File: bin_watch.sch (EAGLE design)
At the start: 100 parts, among them IC1 MEGA48/88/168-MU, J1 USB3100-XX-X_REVB, Q1 32.768kHz, T1 2N7002BKV, T2 2N7002BKV, T3 2N7002BKV, T4 2N7002BKV, T5 PMDT670UPE, T6 PMDT670UPE, T7 PMDT670UPE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

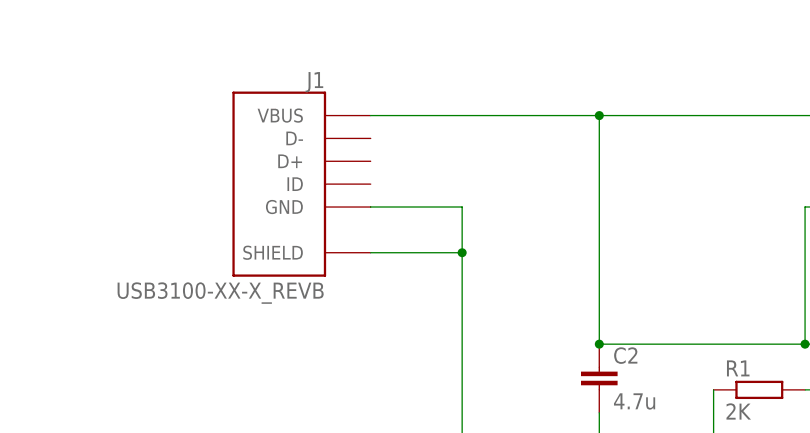
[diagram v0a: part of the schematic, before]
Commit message: Pull resistors for N-channels routed
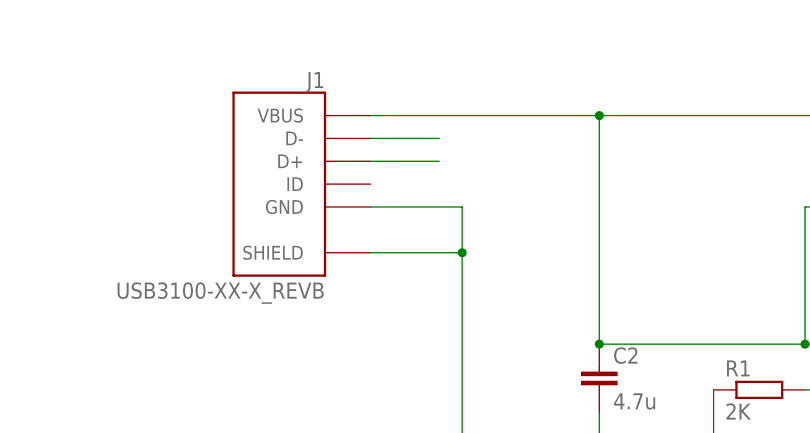
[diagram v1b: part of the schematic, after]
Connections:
- net BLOCK renamed BLOCK5
- net N$1 renamed R_LIGHT5
- net N$2 renamed R_LIGHT6
- net N$4 renamed R_LIGHT7
- net N$5 renamed R_LIGHT4
- net N$6 renamed R_LIGHT0
- net N$7 renamed R_LIGHT1
- net N$8 renamed R_LIGHT2
- net N$9 renamed R_LIGHT3
- net PC0 renamed G_BLOCK0
- net PC1 renamed G_BLOCK1
- net PC2 renamed G_BLOCK2
- net PC3 renamed G_BLOCK3
- net PC4 renamed G_BLOCK4
- net PC5 renamed G_BLOCK5
- net PD0 renamed G_LIGHT0
- net PD1 renamed G_LIGHT1
- net PD2 renamed G_LIGHT2
- net PD3 renamed G_LIGHT3
- net PD4 renamed G_LIGHT4
- net PD5 renamed G_LIGHT5
- net PD6 renamed G_LIGHT6
- net PD7 renamed G_LIGHT7
- new net D_N: J1.D-
- new net D_P: J1.D+
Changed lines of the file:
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@@
 </segment>
 </net>
-<net name="BLOCK" class="3">
+<net name="BLOCK5" class="3">
 <segment>
 <pinref part="D41" gate="G$1" pin="1"/>
@@
 </segment>
 </net>
-<net name="PC0" class="4">
+<net name="G_BLOCK0" class="4">
 <segment>
 <wire x1="139.7" y1="93.98" x2="139.7" y2="106.68" width="0.1524" layer="91"/>
@@
 </segment>
 </net>
-<net name="PC1" class="4">
+<net name="G_BLOCK1" class="4">
 <segment>
 <wire x1="152.4" y1="119.38" x2="152.4" y2="91.44" width="0.1524" layer="91"/>
@@
 </segment>
 </net>
-<net name="PC2" class="4">
+<net name="G_BLOCK2" class="4">
 <segment>
 <wire x1="165.1" y1="106.68" x2="165.1" y2="88.9" width="0.1524" layer="91"/>
@@
 </segment>
 </net>
-<net name="PC3" class="4">
+<net name="G_BLOCK3" class="4">
 <segment>
 <wire x1="177.8" y1="119.38" x2="177.8" y2="86.36" width="0.1524" layer="91"/>
@@
 </segment>
 </net>
-<net name="PC4" class="4">
+<net name="G_BLOCK4" class="4">
 <segment>
 <wire x1="190.5" y1="106.68" x2="190.5" y2="83.82" width="0.1524" layer="91"/>
@@
 </segment>
 </net>
-<net name="PC5" class="4">
+<net name="G_BLOCK5" class="4">
 <segment>
 <wire x1="203.2" y1="119.38" x2="203.2" y2="81.28" width="0.1524" layer="91"/>
@@
 </segment>
 </net>
-<net name="PD0" class="4">
+<net name="G_LIGHT0" class="4">
 <segment>
 <wire x1="177.8" y1="71.12" x2="177.8" y2="43.18" width="0.1524" layer="91"/>
@@
 </segment>
 </net>
-<net name="PD1" class="4">
+<net name="G_LIGHT1" class="4">
 <segment>
 <wire x1="187.96" y1="68.58" x2="187.96" y2="25.4" width="0.1524" layer="91"/>
@@
 </segment>
 </net>
-<net name="PD2" class="4">
+<net name="G_LIGHT2" class="4">
 <segment>
 <wire x1="198.12" y1="66.04" x2="198.12" y2="43.18" width="0.1524" layer="91"/>
@@
 </segment>
 </net>
-<net name="PD3" class="4">
+<net name="G_LIGHT3" class="4">
 <segment>
 <wire x1="208.28" y1="63.5" x2="208.28" y2="25.4" width="0.1524" layer="91"/>
@@
 </segment>
 </net>
-<net name="PD4" class="4">
+<net name="G_LIGHT4" class="4">
 <segment>
 <wire x1="218.44" y1="60.96" x2="218.44" y2="43.18" width="0.1524" layer="91"/>
@@
 </segment>
 </net>
-<net name="PD5" class="4">
+<net name="G_LIGHT5" class="4">
 <segment>
 <wire x1="228.6" y1="58.42" x2="228.6" y2="25.4" width="0.1524" layer="91"/>
@@
 </segment>
 </net>
-<net name="PD6" class="4">
+<net name="G_LIGHT6" class="4">
 <segment>
 <wire x1="238.76" y1="55.88" x2="238.76" y2="43.18" width="0.1524" layer="91"/>
@@
 </segment>
 </net>
-<net name="PD7" class="4">
+<net name="G_LIGHT7" class="4">
 <segment>
 <wire x1="248.92" y1="53.34" x2="248.92" y2="25.4" width="0.1524" layer="91"/>
@@
 </segment>
 </net>
-<net name="N$1" class="0">
+<net name="R_LIGHT5" class="0">
 <segment>
 <wire x1="276.86" y1="58.42" x2="233.68" y2="58.42" width="0.1524" layer="91"/>
@@
 </segment>
 </net>
-<net name="N$2" class="0">
+<net name="R_LIGHT6" class="0">
 <segment>
 <wire x1="261.62" y1="55.88" x2="243.84" y2="55.88" width="0.1524" layer="91"/>
@@
 </segment>
 </net>
-<net name="N$4" class="0">
+<net name="R_LIGHT7" class="0">
 <segment>
 <wire x1="254" y1="33.02" x2="254" y2="53.34" width="0.1524" layer="91"/>
@@
 </segment>
 </net>
-<net name="N$5" class="0">
+<net name="R_LIGHT4" class="0">
 <segment>
 <wire x1="223.52" y1="60.96" x2="269.24" y2="60.96" width="0.1524" layer="91"/>
@@
 </segment>
 </net>
-<net name="N$6" class="0">
+<net name="R_LIGHT0" class="0">
 <segment>
 <pinref part="T1" gate="-1" pin="D"/>
@@
 </segment>
 </net>
-<net name="N$7" class="0">
+<net name="R_LIGHT1" class="0">
 <segment>
 <pinref part="T1" gate="-2" pin="D"/>
@@
 </segment>
 </net>
-<net name="N$8" class="0">
+<net name="R_LIGHT2" class="0">
 <segment>
 <wire x1="203.2" y1="66.04" x2="276.86" y2="66.04" width="0.1524" layer="91"/>
@@
 </segment>
 </net>
-<net name="N$9" class="0">
+<net name="R_LIGHT3" class="0">
 <segment>
 <pinref part="T2" gate="-2" pin="D"/>
@@
 </segment>
 </net>
+<net name="D_N" class="4">
+<segment>
+<pinref part="J1" gate="G$1" pin="D-"/>
+<wire x1="60.96" y1="274.32" x2="68.58" y2="274.32" width="0.1524" layer="91"/>
+</segment>
+</net>
+<net name="D_P" class="4">
+<segment>
+<pinref part="J1" gate="G$1" pin="D+"/>
+<wire x1="60.96" y1="271.78" x2="68.58" y2="271.78" width="0.1524" layer="91"/>
+</segment>
+</net>

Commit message: Pull resistors for N-channels routed
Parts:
- added R19, R20, R21, R22, R23, R24: 1M, rcl:R-EU_R0603
- R13, R14, R15, R16, R17, R18, R2, R3: value 68 -> 1M
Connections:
- net G_BLOCK0: now also R19.1
- net G_BLOCK1: now also R20.1
- net G_BLOCK2: now also R21.1
- net G_BLOCK3: now also R22.1
- net G_BLOCK4: now also R23.1
- net G_BLOCK5: now also R24.1
- net VCC: now also R19.2, R20.2, R21.2, R22.2, R23.2, R24.2
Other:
- moved on the sheet: T5-1, T5-2, T6-1, T6-2, T7-1, T7-2

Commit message: Added solder pads for blocks
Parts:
- removed TP1, TP2, TP3, TP4, TP5, TP6: TPTP07SQ, testpad:TPTP07SQ
- added PAD1, PAD10, PAD11, PAD12, PAD13, PAD14, PAD2, PAD3, PAD4, PAD5, PAD6, PAD7, PAD8, PAD9: (no value), wirepad:SMD2
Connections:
- net BLOCK0: now also PAD9.P
- net BLOCK1: now also PAD10.P
- net BLOCK2: now also PAD11.P
- net BLOCK3: now also PAD12.P
- net BLOCK4: now also PAD13.P
- net BLOCK5: now also PAD14.P
- net GND: no longer TP3.TP
- net LIGHT0: now also PAD1.P
- net LIGHT1: now also PAD2.P
- net LIGHT2: now also PAD3.P
- net LIGHT3: now also PAD4.P
- net LIGHT4: now also PAD5.P
- net LIGHT5: now also PAD6.P
- net LIGHT6: now also PAD7.P
- net LIGHT7: now also PAD8.P
- net MISO: no longer TP6.TP
- net MOSI: no longer TP5.TP
- net RST: no longer TP2.TP
- net SCK: no longer TP4.TP
- net VCC: no longer TP1.TP

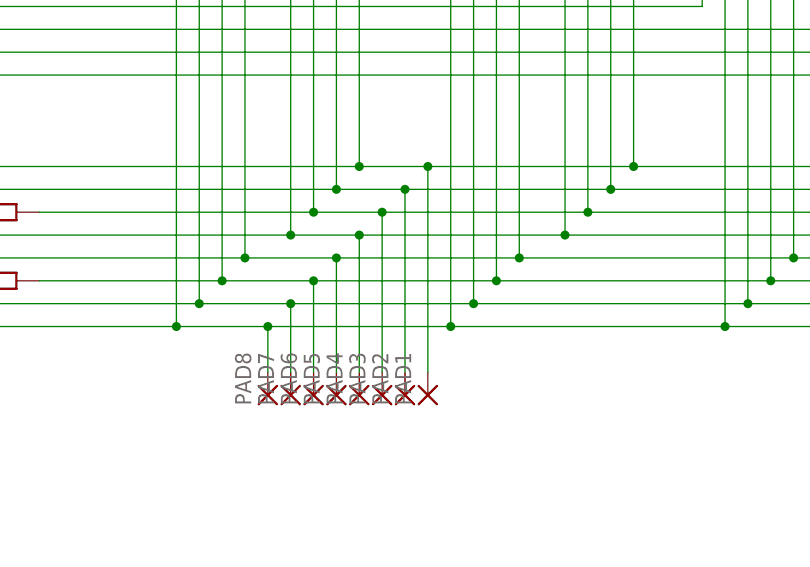
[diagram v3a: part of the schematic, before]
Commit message: Started routing wirepads to drivers
So that the board can be used as a driver for external loads
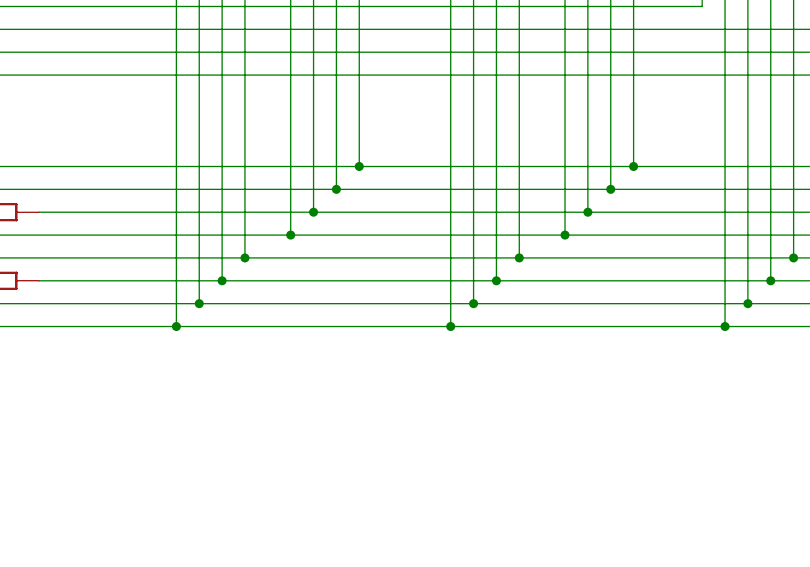
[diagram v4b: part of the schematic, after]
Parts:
- removed PAD1, PAD2, PAD3, PAD4, PAD5, PAD6, PAD7, PAD8: (no value), wirepad:SMD2
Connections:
- net PB0 renamed BTN1
- net PB1 renamed BTN2
- net PB2 renamed BTN3
- net LIGHT0: no longer PAD1.P
- net LIGHT1: no longer PAD2.P
- net LIGHT2: no longer PAD3.P
- net LIGHT3: no longer PAD4.P
- net LIGHT4: no longer PAD5.P
- net LIGHT5: no longer PAD6.P
- net LIGHT6: no longer PAD7.P
- net LIGHT7: no longer PAD8.P
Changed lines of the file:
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@@
 <part name="R24" library="rcl" library_urn="urn:adsk.eagle:library:334" deviceset="R-EU_" device="R0603" package3d_urn="urn:adsk.eagle:package:23555/1" value="1M"/>
 <part name="P+2" library="supply1" library_urn="urn:adsk.eagle:library:371" deviceset="VCC" device=""/>
-<part name="PAD1" library="wirepad" library_urn="urn:adsk.eagle:library:412" deviceset="SMD2" device="" package3d_urn="urn:adsk.eagle:package:30839/1"/>
-<part name="PAD2" library="wirepad" library_urn="urn:adsk.eagle:library:412" deviceset="SMD2" device="" package3d_urn="urn:adsk.eagle:package:30839/1"/>
-<part name="PAD3" library="wirepad" library_urn="urn:adsk.eagle:library:412" deviceset="SMD2" device="" package3d_urn="urn:adsk.eagle:package:30839/1"/>
-<part name="PAD4" library="wirepad" library_urn="urn:adsk.eagle:library:412" deviceset="SMD2" device="" package3d_urn="urn:adsk.eagle:package:30839/1"/>
-<part name="PAD5" library="wirepad" library_urn="urn:adsk.eagle:library:412" deviceset="SMD2" device="" package3d_urn="urn:adsk.eagle:package:30839/1"/>
-<part name="PAD6" library="wirepad" library_urn="urn:adsk.eagle:library:412" deviceset="SMD2" device="" package3d_urn="urn:adsk.eagle:package:30839/1"/>
-<part name="PAD7" library="wirepad" library_urn="urn:adsk.eagle:library:412" deviceset="SMD2" device="" package3d_urn="urn:adsk.eagle:package:30839/1"/>
-<part name="PAD8" library="wirepad" library_urn="urn:adsk.eagle:library:412" deviceset="SMD2" device="" package3d_urn="urn:adsk.eagle:package:30839/1"/>
 <part name="PAD9" library="wirepad" library_urn="urn:adsk.eagle:library:412" deviceset="SMD2" device="" package3d_urn="urn:adsk.eagle:package:30839/1"/>
 <part name="PAD10" library="wirepad" library_urn="urn:adsk.eagle:library:412" deviceset="SMD2" device="" package3d_urn="urn:adsk.eagle:package:30839/1"/>
@@
 <instance part="R24" gate="G$1" x="162.56" y="111.76" rot="R90"/>
 <instance part="P+2" gate="VCC" x="177.8" y="132.08"/>
-<instance part="PAD1" gate="1" x="330.2" y="45.72" rot="R90"/>
-<instance part="PAD2" gate="1" x="327.66" y="45.72" rot="R90"/>
-<instance part="PAD3" gate="1" x="325.12" y="45.72" rot="R90"/>
-<instance part="PAD4" gate="1" x="322.58" y="45.72" rot="R90"/>
-<instance part="PAD5" gate="1" x="320.04" y="45.72" rot="R90"/>
-<instance part="PAD6" gate="1" x="317.5" y="45.72" rot="R90"/>
-<instance part="PAD7" gate="1" x="314.96" y="45.72" rot="R90"/>
-<instance part="PAD8" gate="1" x="312.42" y="45.72" rot="R90"/>
 <instance part="PAD9" gate="1" x="266.7" y="99.06" rot="R270"/>
 <instance part="PAD10" gate="1" x="269.24" y="99.06" rot="R270"/>
@@
 <wire x1="398.78" y1="58.42" x2="368.3" y2="58.42" width="0.1524" layer="91"/>
 <wire x1="368.3" y1="58.42" x2="337.82" y2="58.42" width="0.1524" layer="91"/>
-<wire x1="337.82" y1="58.42" x2="317.5" y2="58.42" width="0.1524" layer="91"/>
-<wire x1="317.5" y1="58.42" x2="307.34" y2="58.42" width="0.1524" layer="91"/>
+<wire x1="337.82" y1="58.42" x2="307.34" y2="58.42" width="0.1524" layer="91"/>
 <wire x1="459.74" y1="111.76" x2="459.74" y2="58.42" width="0.1524" layer="91"/>
 <wire x1="429.26" y1="111.76" x2="429.26" y2="58.42" width="0.1524" layer="91"/>
@@
 <wire x1="307.34" y1="58.42" x2="287.02" y2="58.42" width="0.1524" layer="91"/>
 <pinref part="R10" gate="G$1" pin="2"/>
-<wire x1="317.5" y1="58.42" x2="317.5" y2="48.26" width="0.1524" layer="91"/>
-<junction x="317.5" y="58.42"/>
-<pinref part="PAD6" gate="1" pin="P"/>
 </segment>
 </net>
@@
 <wire x1="396.24" y1="55.88" x2="365.76" y2="55.88" width="0.1524" layer="91"/>
 <wire x1="365.76" y1="55.88" x2="335.28" y2="55.88" width="0.1524" layer="91"/>
-<wire x1="335.28" y1="55.88" x2="314.96" y2="55.88" width="0.1524" layer="91"/>
-<wire x1="314.96" y1="55.88" x2="304.8" y2="55.88" width="0.1524" layer="91"/>
+<wire x1="335.28" y1="55.88" x2="304.8" y2="55.88" width="0.1524" layer="91"/>
 <wire x1="457.2" y1="119.38" x2="457.2" y2="55.88" width="0.1524" layer="91"/>
 <pinref part="D35" gate="G$1" pin="2"/>
@@
 <wire x1="304.8" y1="55.88" x2="271.78" y2="55.88" width="0.1524" layer="91"/>
 <pinref part="R11" gate="G$1" pin="2"/>
-<wire x1="314.96" y1="55.88" x2="314.96" y2="48.26" width="0.1524" layer="91"/>
-<junction x="314.96" y="55.88"/>
-<pinref part="PAD7" gate="1" pin="P"/>
 </segment>
 </net>
@@
 <wire x1="393.7" y1="53.34" x2="363.22" y2="53.34" width="0.1524" layer="91"/>
 <wire x1="363.22" y1="53.34" x2="332.74" y2="53.34" width="0.1524" layer="91"/>
-<wire x1="332.74" y1="53.34" x2="312.42" y2="53.34" width="0.1524" layer="91"/>
-<wire x1="312.42" y1="53.34" x2="302.26" y2="53.34" width="0.1524" layer="91"/>
+<wire x1="332.74" y1="53.34" x2="302.26" y2="53.34" width="0.1524" layer="91"/>
 <wire x1="454.66" y1="127" x2="454.66" y2="53.34" width="0.1524" layer="91"/>
 <wire x1="424.18" y1="127" x2="424.18" y2="53.34" width="0.1524" layer="91"/>
@@
 <wire x1="302.26" y1="53.34" x2="279.4" y2="53.34" width="0.1524" layer="91"/>
 <pinref part="R12" gate="G$1" pin="2"/>
-<wire x1="312.42" y1="53.34" x2="312.42" y2="48.26" width="0.1524" layer="91"/>
-<junction x="312.42" y="53.34"/>
-<pinref part="PAD8" gate="1" pin="P"/>
 </segment>
 </net>
@@
 <wire x1="401.32" y1="60.96" x2="370.84" y2="60.96" width="0.1524" layer="91"/>
 <wire x1="370.84" y1="60.96" x2="340.36" y2="60.96" width="0.1524" layer="91"/>
-<wire x1="340.36" y1="60.96" x2="320.04" y2="60.96" width="0.1524" layer="91"/>
-<wire x1="320.04" y1="60.96" x2="309.88" y2="60.96" width="0.1524" layer="91"/>
+<wire x1="340.36" y1="60.96" x2="309.88" y2="60.96" width="0.1524" layer="91"/>
 <wire x1="462.28" y1="104.14" x2="462.28" y2="60.96" width="0.1524" layer="91"/>
 <pinref part="D33" gate="G$1" pin="2"/>
@@
 <pinref part="R9" gate="G$1" pin="2"/>
 <wire x1="279.4" y1="60.96" x2="309.88" y2="60.96" width="0.1524" layer="91"/>
-<wire x1="320.04" y1="60.96" x2="320.04" y2="48.26" width="0.1524" layer="91"/>
-<junction x="320.04" y="60.96"/>
-<pinref part="PAD5" gate="1" pin="P"/>
 </segment>
 </net>
@@
 <wire x1="414.02" y1="71.12" x2="383.54" y2="71.12" width="0.1524" layer="91"/>
 <wire x1="383.54" y1="71.12" x2="353.06" y2="71.12" width="0.1524" layer="91"/>
-<wire x1="353.06" y1="71.12" x2="330.2" y2="71.12" width="0.1524" layer="91"/>
-<wire x1="330.2" y1="71.12" x2="322.58" y2="71.12" width="0.1524" layer="91"/>
+<wire x1="353.06" y1="71.12" x2="322.58" y2="71.12" width="0.1524" layer="91"/>
 <wire x1="444.5" y1="104.14" x2="444.5" y2="71.12" width="0.1524" layer="91"/>
 <junction x="444.5" y="71.12"/>
@@
 <pinref part="R5" gate="G$1" pin="2"/>
 <wire x1="271.78" y1="71.12" x2="322.58" y2="71.12" width="0.1524" layer="91"/>
-<wire x1="330.2" y1="71.12" x2="330.2" y2="48.26" width="0.1524" layer="91"/>
-<junction x="330.2" y="71.12"/>
-<pinref part="PAD1" gate="1" pin="P"/>
 </segment>
 </net>
@@
 <wire x1="411.48" y1="68.58" x2="381" y2="68.58" width="0.1524" layer="91"/>
 <wire x1="381" y1="68.58" x2="350.52" y2="68.58" width="0.1524" layer="91"/>
-<wire x1="350.52" y1="68.58" x2="327.66" y2="68.58" width="0.1524" layer="91"/>
-<wire x1="327.66" y1="68.58" x2="320.04" y2="68.58" width="0.1524" layer="91"/>
+<wire x1="350.52" y1="68.58" x2="320.04" y2="68.58" width="0.1524" layer="91"/>
 <wire x1="441.96" y1="111.76" x2="441.96" y2="68.58" width="0.1524" layer="91"/>
 <junction x="441.96" y="68.58"/>
@@
 <wire x1="320.04" y1="68.58" x2="279.4" y2="68.58" width="0.1524" layer="91"/>
 <pinref part="R6" gate="G$1" pin="2"/>
-<wire x1="327.66" y1="48.26" x2="327.66" y2="68.58" width="0.1524" layer="91"/>
-<junction x="327.66" y="68.58"/>
-<pinref part="PAD2" gate="1" pin="P"/>
 </segment>
 </net>
@@
 <wire x1="408.94" y1="66.04" x2="378.46" y2="66.04" width="0.1524" layer="91"/>
 <wire x1="378.46" y1="66.04" x2="347.98" y2="66.04" width="0.1524" layer="91"/>
-<wire x1="347.98" y1="66.04" x2="325.12" y2="66.04" width="0.1524" layer="91"/>
-<wire x1="325.12" y1="66.04" x2="317.5" y2="66.04" width="0.1524" layer="91"/>
+<wire x1="347.98" y1="66.04" x2="317.5" y2="66.04" width="0.1524" layer="91"/>
 <wire x1="439.42" y1="119.38" x2="439.42" y2="66.04" width="0.1524" layer="91"/>
 <junction x="439.42" y="66.04"/>
@@
 <pinref part="R7" gate="G$1" pin="2"/>
 <wire x1="287.02" y1="66.04" x2="317.5" y2="66.04" width="0.1524" layer="91"/>
-<wire x1="325.12" y1="66.04" x2="325.12" y2="48.26" width="0.1524" layer="91"/>
-<junction x="325.12" y="66.04"/>
-<pinref part="PAD3" gate="1" pin="P"/>
 </segment>
 </net>
@@
 <wire x1="406.4" y1="63.5" x2="375.92" y2="63.5" width="0.1524" layer="91"/>
 <wire x1="375.92" y1="63.5" x2="345.44" y2="63.5" width="0.1524" layer="91"/>
-<wire x1="345.44" y1="63.5" x2="322.58" y2="63.5" width="0.1524" layer="91"/>
-<wire x1="322.58" y1="63.5" x2="314.96" y2="63.5" width="0.1524" layer="91"/>
+<wire x1="345.44" y1="63.5" x2="314.96" y2="63.5" width="0.1524" layer="91"/>
 <wire x1="436.88" y1="127" x2="436.88" y2="63.5" width="0.1524" layer="91"/>
 <junction x="436.88" y="63.5"/>
@@
 <wire x1="314.96" y1="63.5" x2="271.78" y2="63.5" width="0.1524" layer="91"/>
 <pinref part="R8" gate="G$1" pin="2"/>
-<wire x1="322.58" y1="63.5" x2="322.58" y2="48.26" width="0.1524" layer="91"/>
-<junction x="322.58" y="63.5"/>
-<pinref part="PAD4" gate="1" pin="P"/>
-</segment>
-</net>
-<net name="PB0" class="4">
+</segment>
+</net>
+<net name="BTN1" class="4">
 <segment>
 <pinref part="S1" gate="G$1" pin="1"/>
@@
 </segment>
 </net>
-<net name="PB1" class="4">
+<net name="BTN2" class="4">
 <segment>
 <pinref part="S2" gate="G$1" pin="1"/>
@@
 </segment>
 </net>
-<net name="PB2" class="4">
+<net name="BTN3" class="4">
 <segment>
 <pinref part="S3" gate="G$1" pin="1"/>
